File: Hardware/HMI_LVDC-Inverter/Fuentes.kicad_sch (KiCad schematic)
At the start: 41 parts, among them U3 AP64100SP-13, U4 AMS1117-3.3, U5 B1205S-2WR2, U6 AMS1117-3.3, U7 B1205S-2WR2, U8 TPS74633PQWDRBRQ1

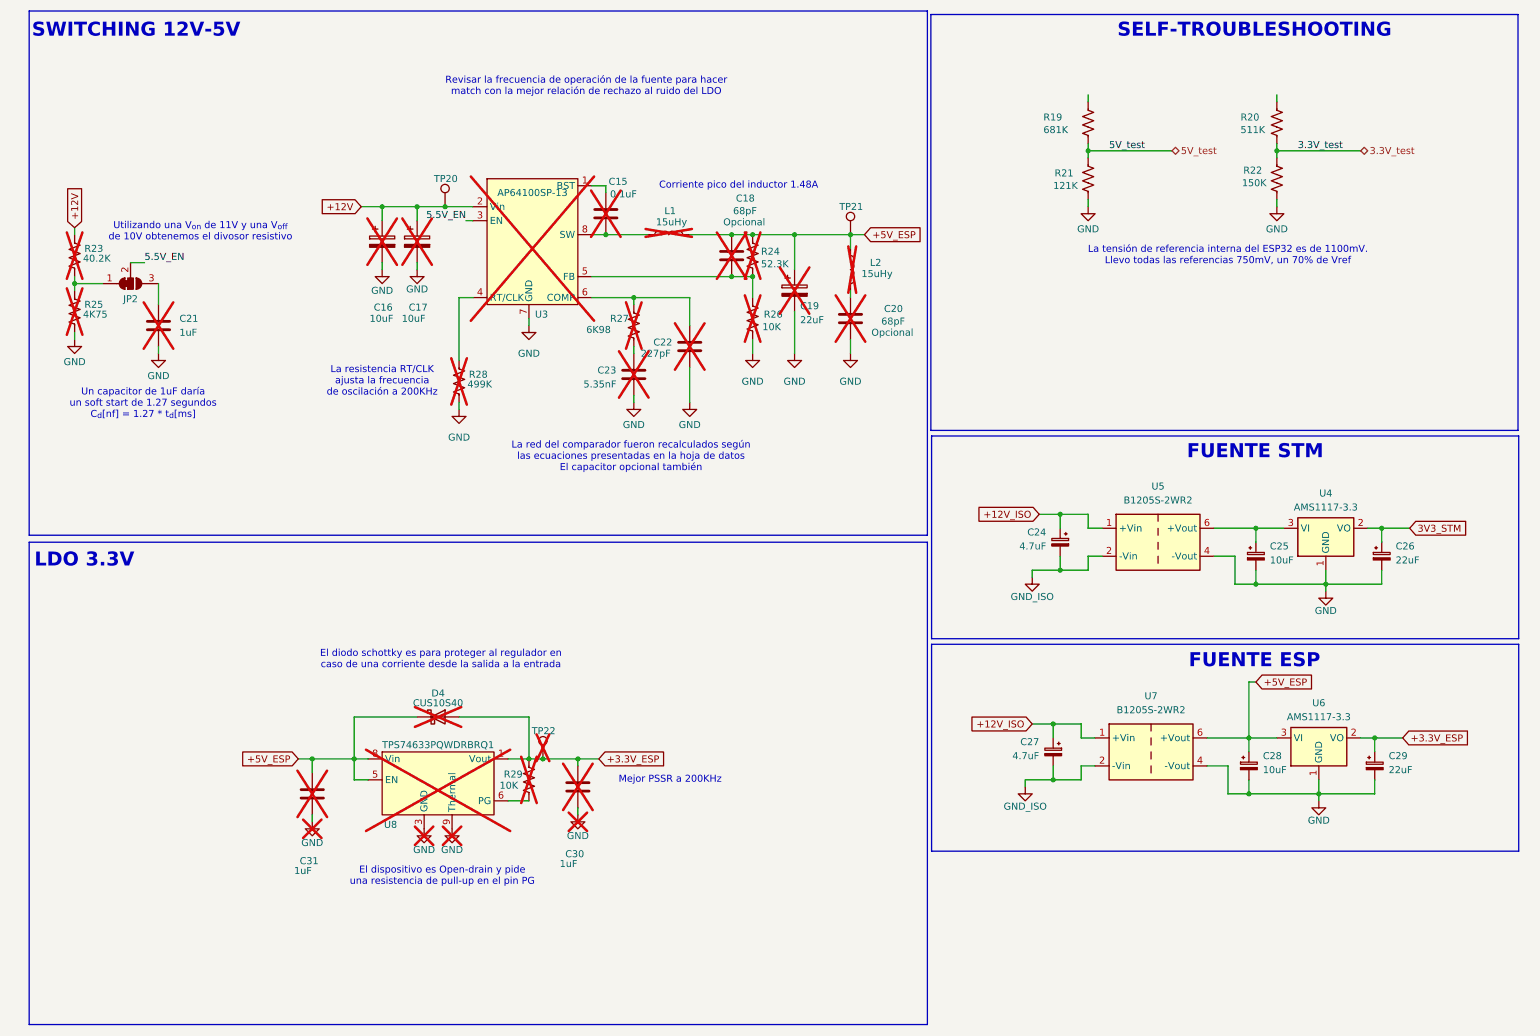
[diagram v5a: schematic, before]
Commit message: Avances en el PCB, arreglos en el esquema y agregado de borneras de gabinete
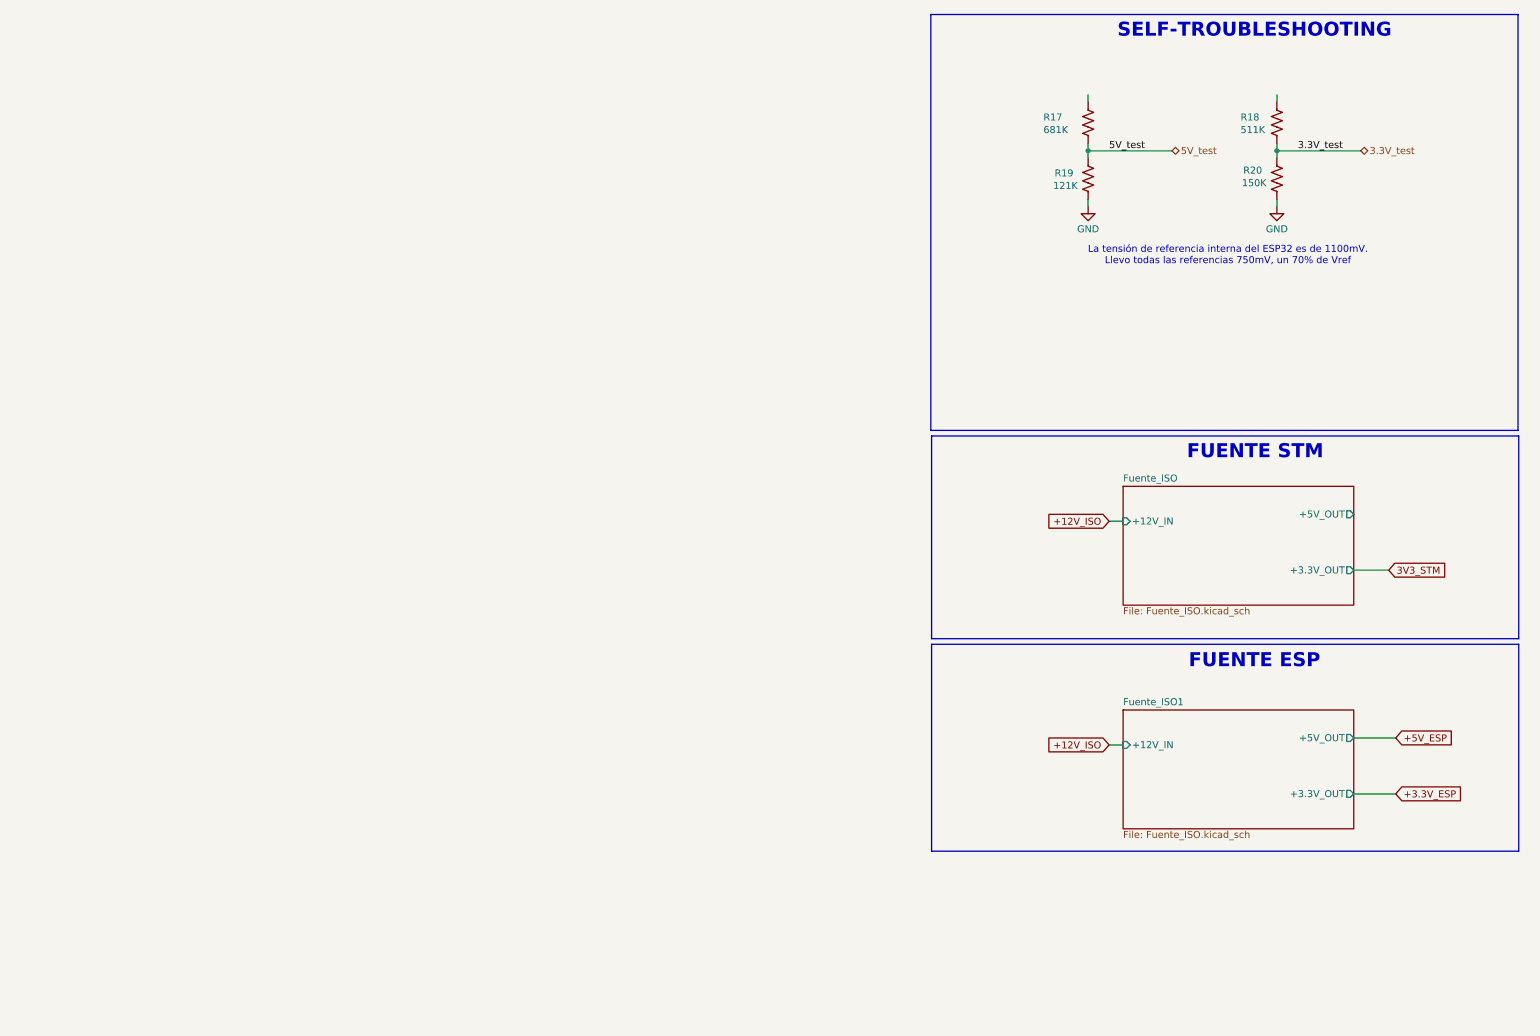
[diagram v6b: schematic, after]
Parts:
- removed C15: 0.1uF, Capacitor_SMD:C_0603_1608Metric, symbol Device:C
- removed C16, C17: 10uF, symbol Device:C_Polarized
- removed C18, C20: 68pF, Capacitor_SMD:C_0603_1608Metric, symbol Device:C
- removed C19: 22uF, Capacitor_SMD:C_1206_3216Metric, symbol Device:C_Polarized
- removed C21, C30, C31: 1uF, symbol Device:C
- removed C22: 227pF, symbol Device:C
- removed C23: 5.35nF, symbol Device:C
- removed C24, C27: 4.7uF, Capacitor_SMD:C_0603_1608Metric, symbol Device:C_Polarized_Small
- removed C25, C28: 10uF, Capacitor_SMD:CP_Elec_4x5.4, symbol Device:C_Polarized_Small
- removed C26, C29: 22uF, Capacitor_SMD:CP_Elec_4x5.4, symbol Device:C_Polarized_Small
- removed D4: CUS10S40, Diode_SMD:D_SOD-323F, symbol Device:D_Schottky
- removed JP2: SolderJumper_3_Bridged12, Jumper:SolderJumper-3_P1.3mm_Bridged12_Pad1.0x1.5mm, symbol Jumper:SolderJumper_3_Bridged12
- removed L1, L2: 15uHy, symbol Device:L
- removed R23: 40.2K, symbol Device:R_US
- removed R24: 52.3K, symbol Device:R_US
- removed R25: 4K75, symbol Device:R_US
- removed R26, R29: 10K, symbol Device:R_US
- removed R27: 6K98, symbol Device:R_US
- removed R28: 499K, symbol Device:R_US
- removed TP20, TP21, TP22: TestPoint, symbol Connector:TestPoint
- removed U3: AP64100SP-13, Package_SO:Diodes_SO-8EP, symbol Personal:AP64100Q
- removed U4, U6: AMS1117-3.3, Package_TO_SOT_SMD:SOT-223-3_TabPin2, symbol Regulator_Linear:AMS1117-3.3
- removed U5, U7: B1205S-2WR2, Converter_DCDC:Converter_DCDC_TRACO_TMA-05xxS_12xxS_Single_THT, symbol Converter_DCDC:TMA-1205S
- removed U8: TPS74633PQWDRBRQ1, Package_SON:VSON-8-1EP_3x3mm_P0.65mm_EP1.65x2.4mm_ThermalVias, symbol Personal:TPS76833QDR
- renumbered R19 to R17, R20 to R18, R21 to R19, R22 to R20
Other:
- added sheet Fuente_ISO (Fuente_ISO.kicad_sch)
- added sheet Fuente_ISO1 (Fuente_ISO.kicad_sch)
- note removed: "Corriente pico del inductor 1.48A"
- note removed: "El diodo schottky es para proteger al regulador en caso de una corriente desde la salida a la entrada"
- note removed: "El dispositivo es Open-drain y pide una resistencia de pull-up en el pin PG"
- note removed: "LDO 3.3V"
- note removed: "La red del comparador fueron recalculados según las ecuaciones presentadas en la hoja de datos El capacitor opcional también"
- note removed: "La resistencia RT/CLK ajusta la frecuencia de oscilación a 200KHz"
- note removed: "Mejor PSSR a 200KHz"
- note removed: "Revisar la frecuencia de operación de la fuente para hacer match con la mejor relación de rechazo al ruido del LDO"
- note removed: "SWITCHING 12V-5V"
- note removed: "Un capacitor de 1uF daría un soft start de 1.27 segundos C_{d}[nf] = 1.27 * t_{d}[ms]"
- note removed: "Utilizando una V_{on} de 11V y una V_{off} de 10V obtenemos el divosor resistivo"

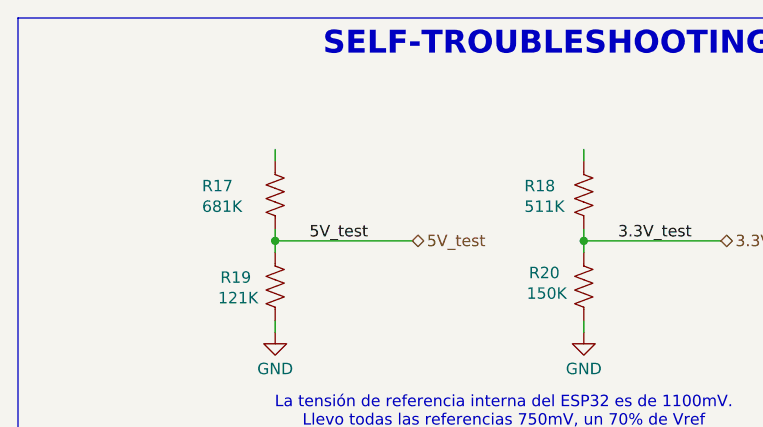
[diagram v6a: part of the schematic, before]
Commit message: Falta resolver los pulsadores
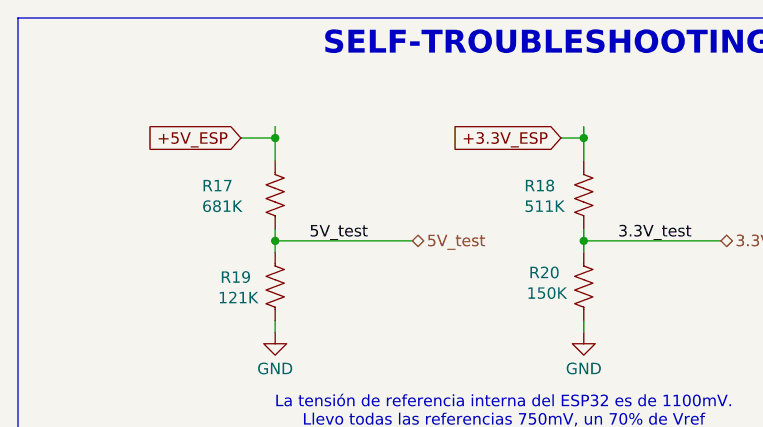
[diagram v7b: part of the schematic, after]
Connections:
- net +3.3V_ESP: now also R18.1
- net +5V_ESP: now also R17.1
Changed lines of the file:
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@@
+	)
+	(junction
+		(at 240.03 26.67)
+		(diameter 0)
+		(color 0 0 0 0)
+	)
+	(junction
+		(at 205.74 26.67)
+		(diameter 0)
+		(color 0 0 0 0)
 	)
 	(junction
@@
 	(wire
 		(pts
-			(xy 205.74 27.94) (xy 205.74 29.21)
+			(xy 205.74 25.4) (xy 205.74 26.67)
 		)
 		(stroke
@@
 	(wire
 		(pts
+			(xy 240.03 26.67) (xy 240.03 29.21)
+		)
+		(stroke
+			(width 0)
+			(type default)
+		)
+	)
+	(wire
+		(pts
+			(xy 205.74 26.67) (xy 205.74 29.21)
+		)
+		(stroke
+			(width 0)
+			(type default)
+		)
+	)
+	(wire
+		(pts
 			(xy 209.55 146.05) (xy 212.09 146.05)
 		)
@@
 	(wire
 		(pts
-			(xy 240.03 27.94) (xy 240.03 29.21)
+			(xy 240.03 25.4) (xy 240.03 26.67)
 		)
 		(stroke
@@
 	(wire
 		(pts
+			(xy 201.93 26.67) (xy 205.74 26.67)
+		)
+		(stroke
+			(width 0)
+			(type default)
+		)
+	)
+	(wire
+		(pts
 			(xy 254 114.3) (xy 260.35 114.3)
 		)
@@
 		(pts
 			(xy 254 144.78) (xy 261.62 144.78)
+		)
+		(stroke
+			(width 0)
+			(type default)
+		)
+	)
+	(wire
+		(pts
+			(xy 237.49 26.67) (xy 240.03 26.67)
 		)
 		(stroke
@@
 		)
 	)
+	(global_label "+5V_ESP"
+		(shape input)
+		(at 201.93 26.67 180)
+		(fields_autoplaced yes)
+		(effects
+			(font
+				(size 1.27 1.27)
+			)
+			(justify right)
+		)
+		(property "Intersheetrefs" "${INTERSHEET_REFS}"
+			(at 190.4782 26.67 0)
+			(effects
+				(font
+					(size 1.27 1.27)
+				)
+				(justify right)
+				(hide yes)
+			)
+		)
+	)
+	(global_label "+3.3V_ESP"
+		(shape input)
+		(at 237.49 26.67 180)
+		(fields_autoplaced yes)
+		(effects
+			(font
+				(size 1.27 1.27)
+			)
+			(justify right)
+		)
+		(property "Intersheetrefs" "${INTERSHEET_REFS}"
+			(at 224.2239 26.67 0)
+			(effects
+				(font
+					(size 1.27 1.27)
+				)
+				(justify right)
+				(hide yes)
+			)
+		)
+	)
 	(global_label "+12V_ISO"
 		(shape input)
@@
 		(length 2.54)
 		(shape round)
-		(at 240.03 27.94 0)
+		(at 240.03 25.4 0)
 		(effects
 			(font
@@
 		)
 		(property "Netclass" "+3.3V_ESP"
-			(at 237.236 23.368 0)
+			(at 237.236 20.828 0)
 			(effects
 				(font
@@
 		)
 		(property "Component Class" ""
-			(at -55.88 -39.37 0)
+			(at -55.88 -41.91 0)
 			(effects
 				(font
@@
 		(length 2.54)
 		(shape round)
-		(at 205.74 27.94 0)
+		(at 205.74 25.4 0)
 		(effects
 			(font
@@
 		)
 		(property "Netclass" "+5V_ESP"
-			(at 203.962 23.368 0)
+			(at 203.962 20.828 0)
 			(effects
 				(font
@@
 		)
 		(property "Component Class" ""
-			(at -90.17 -39.37 0)
-			(effects
-				(font
+			(at -90.17 -41.91 0)
+			(effects
+				(font
